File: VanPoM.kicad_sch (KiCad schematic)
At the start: 81 parts, among them IC2 UCC27517DBVR, J1 Socket_ESP32-WROOM-32-NODEMCU, J2 OSTT7020150, J3 OSTT7020150, J4 OSTT7020150, J5 OSTT7020150, Q1 CSD18540Q5B, Q10 CSD18540Q5B, Q2 IPP055N03L G, Q3 IPP120P04P4L03AKSA2, Q4 CSD19531Q5A, Q5 CSD19531Q5A, Q6 CSD19531Q5A, Q7 CSD19531Q5A, Q8 CSD18540Q5B, Q9 CSD18540Q5B, U1 BQ34Z100-R2, U2 LM5109BMA/NOPB, U3 LM5109BMA/NOPB, U4 INA240A2D, U5 INA240A2D, U6 INA240A2D, U7 LM74700, U8 LM74700

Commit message: init
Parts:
- removed J1: Socket_ESP32-WROOM-32-NODEMCU, Connector_PinSocket_2.54mm:PinSocket_1x19_P2.54mm_Vertical, symbol Perso:Socket_ESP32-WROOM-32-NODEMCU
- added C29: 47u, symbol Device:C
- added C30: 10u, symbol Perso:Cv
- added C31: 1u, symbol Perso:Cv
- added C32: 0.022u, symbol Perso:Cv
- added C33: 10n, symbol Device:C
- added C34, C35, C43, C44, C45: 1u, symbol Device:C
- added C36, C37, C38, C39, C40, C41, C42: 0.1u, symbol Device:C
- added D10, D11, D12, D13, D14, D15, D16, D17, D18, D19, D20, D21, D22, D23, D24, D25, D7, D8, D9: PESD2USB3UXT-QR, Package_TO_SOT_SMD:SOT-23, symbol Perso:PESD2USB3UXT-QR
- added D6: B1100B-13-F, symbol Device:D_Schottky
- added IC1: TLV70433DBVT, SOT95P280X145-5N, symbol Perso:TLV70433DBVT
- added IC3: SN74LV4052APWR, Package_SO:TSSOP-16_4.4x5mm_P0.65mm, symbol Perso:SN74LV4052APWR
- added J1: Conn_03x26_Row_Letter_First, Perso:PinHeader_3x25_P2.54mm_Vertical, symbol Perso:Conn_03x26_Row_Letter_First
- added J10: UART3, symbol Connector:Conn_01x04_Pin
- added J11: UART4, symbol Connector:Conn_01x04_Pin
- added J6: OSTT7020150, Perso:CONN2_OSTT7020150_OST, symbol Perso:OSTT7020150
- added J8: UART1, symbol Connector:Conn_01x04_Pin
- added J9: UART2, symbol Connector:Conn_01x04_Pin
- added L3: 220u, symbol Device:L
- added Q11: CSD18540Q5B, Package_TO_SOT_SMD:TDSON-8-1, symbol Transistor_FET:CSD18540Q5B
- added R17: 430k, symbol Device:R
- added R18: 169k, symbol Device:R
- added R19: 3.00k, symbol Device:R
- added R20: 1.00k, symbol Device:R
- added R21: 3.00, symbol Device:R
- added R22, R23, R24, R25: 1.8M, symbol Device:R
- added R26, R27, R28, R29: 200k, symbol Device:R
- added U10: LM5009MM, Package_SO:MSOP-8_3x3mm_P0.65mm, symbol Regulator_Switching:LM5009MM
- added U11: ESP32-S3-DEVKITC-1-N8R2, ESP32-S3-DEVKITC-1-N8R2:XCVR_ESP32-S3-DEVKITC-1-N8R2, symbol Perso:ESP32-S3-DEVKITC-1-N8R2
- added U12: TLA2528IRTER, Perso:WQFN16_RTE_TEX-L, symbol Perso:TLA2528IRTER
- added U13, U14, U15, U16, U17: TVS3300DRV, Package_SON:WSON-6-1EP_2x2mm_P0.65mm_EP1x1.6mm, symbol Perso:TVS3300DRV
- added U9: LM74700, Package_TO_SOT_SMD:SOT-23-6, symbol Power_Management:LM74700
- Q2: value IPP055N03L G -> NX7002AK,215
- Q3: value IPP120P04P4L03AKSA2 -> BSS84W-7-F
- R2: value ~ -> 330k
- R3: value ~ -> 240k
- R4: value ~ -> 390k
- R5: value ~ -> 30k
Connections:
- net +10V: now also C33.1, C34.1, IC1.2 (IN), R21.2
- net +3V3: now also C35.1, D20.1 (K), D20.2 (K), IC1.3 (OUT), IC3.16 (VCC), J1.b1 (Pin_b1), J1.b10 (Pin_b10), J1.b11 (Pin_b11), J1.b12 (Pin_b12), J1.b13 (Pin_b13), J1.b14 (Pin_b14), J1.b15 (Pin_b15), J1.b16 (Pin_b16), J1.b17 (Pin_b17), J1.b18 (Pin_b18), J1.b19 (Pin_b19), J1.b2 (Pin_b2), J1.b20 (Pin_b20), J1.b21 (Pin_b21), J1.b22 (Pin_b22), J1.b23 (Pin_b23), J1.b24 (Pin_b24), J1.b25 (Pin_b25), J1.b26 (Pin_b26), J1.b3 (Pin_b3), J1.b4 (Pin_b4), J1.b5 (Pin_b5), J1.b6 (Pin_b6), J1.b7 (Pin_b7), J1.b8 (Pin_b8), J1.b9 (Pin_b9), J10.1 (Pin_1), J11.1 (Pin_1), J8.1 (Pin_1), J9.1 (Pin_1), U11.J1_1 (3V3), U11.J1_2 (3V3)
- net BAT+: now also R25.1, U16.4 (IN), U16.5 (IN), U16.6 (IN)
- net B_I: now also C40.1, U12.5 (AIN6/GPIO6)
- net Bu_I: now also C41.1, U12.4 (AIN5/GPIO5)
- net GNDREF: now also C30.1, C31.1, C33.2, C34.2, C35.2, C36.2, C37.2, C38.2, C39.2, C40.2, C41.2, C42.2, C43.2, C44.2, C45.2, D21.1 (K), D21.2 (K), D6.2 (A), IC1.1 (GND), IC1.4 (NC_1), IC1.5 (NC_2), IC3.7 (GND_1), IC3.8 (GND_2), J1.a1 (Pin_a1), J1.a10 (Pin_a10), J1.a11 (Pin_a11), J1.a12 (Pin_a12), J1.a13 (Pin_a13), J1.a14 (Pin_a14), J1.a15 (Pin_a15), J1.a16 (Pin_a16), J1.a17 (Pin_a17), J1.a18 (Pin_a18), J1.a19 (Pin_a19), J1.a2 (Pin_a2), J1.a20 (Pin_a20), J1.a21 (Pin_a21), J1.a22 (Pin_a22), J1.a23 (Pin_a23), J1.a24 (Pin_a24), J1.a25 (Pin_a25), J1.a26 (Pin_a26), J1.a3 (Pin_a3), J1.a4 (Pin_a4), J1.a5 (Pin_a5), J1.a6 (Pin_a6), J1.a7 (Pin_a7), J1.a8 (Pin_a8), J1.a9 (Pin_a9), J10.4 (Pin_4), J11.4 (Pin_4), J6.2 (Pin_2), J8.4 (Pin_4), J9.4 (Pin_4), R18.1, R20.2, R26.2, R27.2, R28.2, R29.2, U10.4 (RTN), U11.J1_22 (GND), U11.J3_1 (GND), U11.J3_21 (GND), U11.J3_22 (GND), U12.17 (GND), U12.9 (GND), U17.4 (IN), U17.5 (IN), U17.6 (IN), U9.2 (GND)
- net L_EN: now also U11.J1_15 (GPIO9)
- net P+: now also U13.4 (IN), U13.5 (IN), U13.6 (IN)
- net P_EN: now also U11.J1_18 (GPIO12)
- net P_I: now also C42.1, U12.3 (AIN4/GPIO4)
- net P_S-: now also R24.1
- net SCL: now also U11.J1_17 (GPIO11), U12.14 (SDA)
- net SDA: now also U11.J1_16 (GPIO10), U12.13 (SCL)
- net S_EN: now also U11.J1_19 (GPIO13)
- net V_IN: now also C30.2, Q11.5 (D), R17.1, U10.8 (VIN), U9.4 (CATHODE)
- net V_S: now reaches C20.2, J5.1 (Pin_1), Q8.1 (S), Q8.2 (S), Q8.3 (S), R16.1, U8.6 (ANODE)
- net V_S: now also R22.1, U14.4 (IN), U14.5 (IN), U14.6 (IN)
- new net: L3.2, R19.1, R21.1
- new net: D6.1 (K), R19.2, R20.1, U10.5 (FB)
- new net: C37.1, R24.2, R27.1, U12.1 (AIN2/GPIO2)
- new net: C44.1, U12.10 (DVDD)
- new net: C39.1, R22.2, R29.1, U12.15 (AIN0/GPIO0)
- new net: C38.1, R23.2, R28.1, U12.16 (AIN1/GPIO1)
- new net: C36.1, R25.2, R26.1, U12.2 (AIN3/GPIO3)
- new net: C43.1, U12.7 (AVDD)
- new net: C45.1, U12.8 (DECAP)
- new net: C29.1, U9.1 (VCAP)
- new net: U14.1 (GND), U14.2 (GND), U14.3 (GND), U14.7 (GND)
- new net: C32.1, U10.2 (BST)
- new net: C32.2, L3.1, U10.1 (SW)
- new net: Q11.4 (G), U9.5 (GATE)
- new net: C31.2, U10.7 (VCC)
- new net: R17.2, U10.6 (RON/SD)
- new net: R18.2, U10.3 (RCL)
- new net: U13.1 (GND), U13.2 (GND), U13.3 (GND), U13.7 (GND)
- new net A_EN: U11.J1_20 (GPIO14), U9.3 (EN)
- new net GPIO0: D10.1 (K), J1.c20 (Pin_c20), U11.J3_14 (GPIO0)
- new net GPIO1: D15.1 (K), J1.c10 (Pin_c10), U11.J3_4 (GPIO1)
- new net GPIO15: D18.2 (K), J1.c3 (Pin_c3), U11.J1_8 (GPIO15)
- new net GPIO16: D18.1 (K), J1.c4 (Pin_c4), U11.J1_9 (GPIO16)
- new net GPIO17: D17.2 (K), J1.c5 (Pin_c5), U11.J1_10 (GPIO17)
- new net GPIO18: D17.1 (K), J1.c6 (Pin_c6), U11.J1_11 (GPIO18)
- new net GPIO19: D7.1 (K), J1.c26 (Pin_c26), U11.J3_20 (USB_D-/GPIO19)
- new net GPIO2: D14.2 (K), J1.c11 (Pin_c11), U11.J3_5 (GPIO2)
- new net GPIO20: D7.2 (K), J1.c25 (Pin_c25), U11.J3_19 (USB_D+/GPIO20)
- new net GPIO21: D8.1 (K), J1.c24 (Pin_c24), U11.J3_18 (GPIO21)
- new net GPIO3: D16.1 (K), J1.c8 (Pin_b8), U11.J1_13 (GPIO3)
- new net GPIO35: D10.2 (K), J1.c19 (Pin_c19), U11.J3_13 (GPIO35)
- new net GPIO36: D11.1 (K), J1.c18 (Pin_c18), U11.J3_12 (GPIO36)
- new net GPIO37: D11.2 (K), J1.c17 (Pin_c17), U11.J3_11 (GPIO37)
- new net GPIO38: D12.1 (K), J1.c16 (Pin_c16), U11.J3_10 (GPIO38)
- new net GPIO39: D12.2 (K), J1.c15 (Pin_c15), U11.J3_9 (MTCK/GPIO39)
- new net GPIO40: D13.1 (K), J1.c14 (Pin_c14), U11.J3_8 (MTDO/GPIO40)
- new net GPIO41: D13.2 (K), J1.c13 (Pin_c13), U11.J3_7 (MTDI/GPIO41)
- new net GPIO42: D14.1 (K), J1.c12 (Pin_c12), U11.J3_6 (MTMS/GPIO42)
- new net GPIO45: D9.2 (K), J1.c21 (Pin_c21), U11.J3_15 (GPIO45)
- new net GPIO46: D15.2 (K), J1.c9 (Pin_c9), U11.J1_14 (GPIO46)
- new net GPIO47: D8.2 (K), J1.c23 (Pin_c23), U11.J3_17 (GPIO47)
- new net GPIO48: D9.1 (K), J1.c22 (Pin_c22), U11.J3_16 (GPIO48)
- new net GPIO6: D19.2 (K), J1.c1 (Pin_c1), U11.J1_6 (GPIO6)
- new net GPIO7: D19.1 (K), J1.c2 (Pin_c2), U11.J1_7 (GPIO7)
- new net GPIO8: D16.2 (K), J1.c7 (Pin_b7), U11.J1_12 (GPIO8)
- new net RX0: IC3.12 (1Y0)
- new net RX1: D22.2 (K), IC3.14 (1Y1), J8.2 (Pin_2)
- new net RX2: D23.2 (K), IC3.15 (1Y2), J9.2 (Pin_2)
- new net RX3: D24.2 (K), IC3.11 (1Y3), J10.2 (Pin_2)
- new net RX4: D25.2 (K), J11.2 (Pin_2)
- new net RX_COM: IC3.13 (1-COM), U11.J3_3 (U0RXD/GPIO44)
- new net TVS: U15.1 (GND), U15.2 (GND), U15.3 (GND), U15.7 (GND), U16.1 (GND), U16.2 (GND), U16.3 (GND), U16.7 (GND), U17.1 (GND), U17.2 (GND), U17.3 (GND), U17.7 (GND)
- new net TVS_3v3: D10.3 (A), D11.3 (A), D12.3 (A), D13.3 (A), D14.3 (A), D15.3 (A), D16.3 (A), D17.3 (A), D18.3 (A), D19.3 (A), D20.3 (A), D21.3 (A), D22.3 (A), D23.3 (A), D24.3 (A), D25.3 (A), D7.3 (A), D8.3 (A), D9.3 (A)
- new net TX0: IC3.1 (2Y0)
- new net TX1: D22.1 (K), IC3.5 (2Y1), J8.3 (Pin_3)
- new net TX2: D23.1 (K), IC3.2 (2Y2), J9.3 (Pin_3)
- new net TX3: D24.1 (K), IC3.4 (2Y3), J10.3 (Pin_3)
- new net TX4: D25.1 (K), J11.3 (Pin_3)
- new net TX_COM: IC3.3 (2-COM), U11.J3_2 (U0TXD/GPIO43)
- new net UART_A0: IC3.10 (A), U11.J1_4 (GPIO4)
- new net UART_A1: IC3.9 (B), U11.J1_5 (GPIO5)
- new net V_A: C29.2, J6.1 (Pin_1), Q11.1 (S), Q11.2 (S), Q11.3 (S), R23.1, U15.4 (IN), U15.5 (IN), U15.6 (IN), U9.6 (ANODE)
- no-connect marks 0 -> 2
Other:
- note added: "Car generator"
- moved on the sheet: C1, C10, C11, C12, C13, C14, C15, C16, C17, C18, C19, C2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

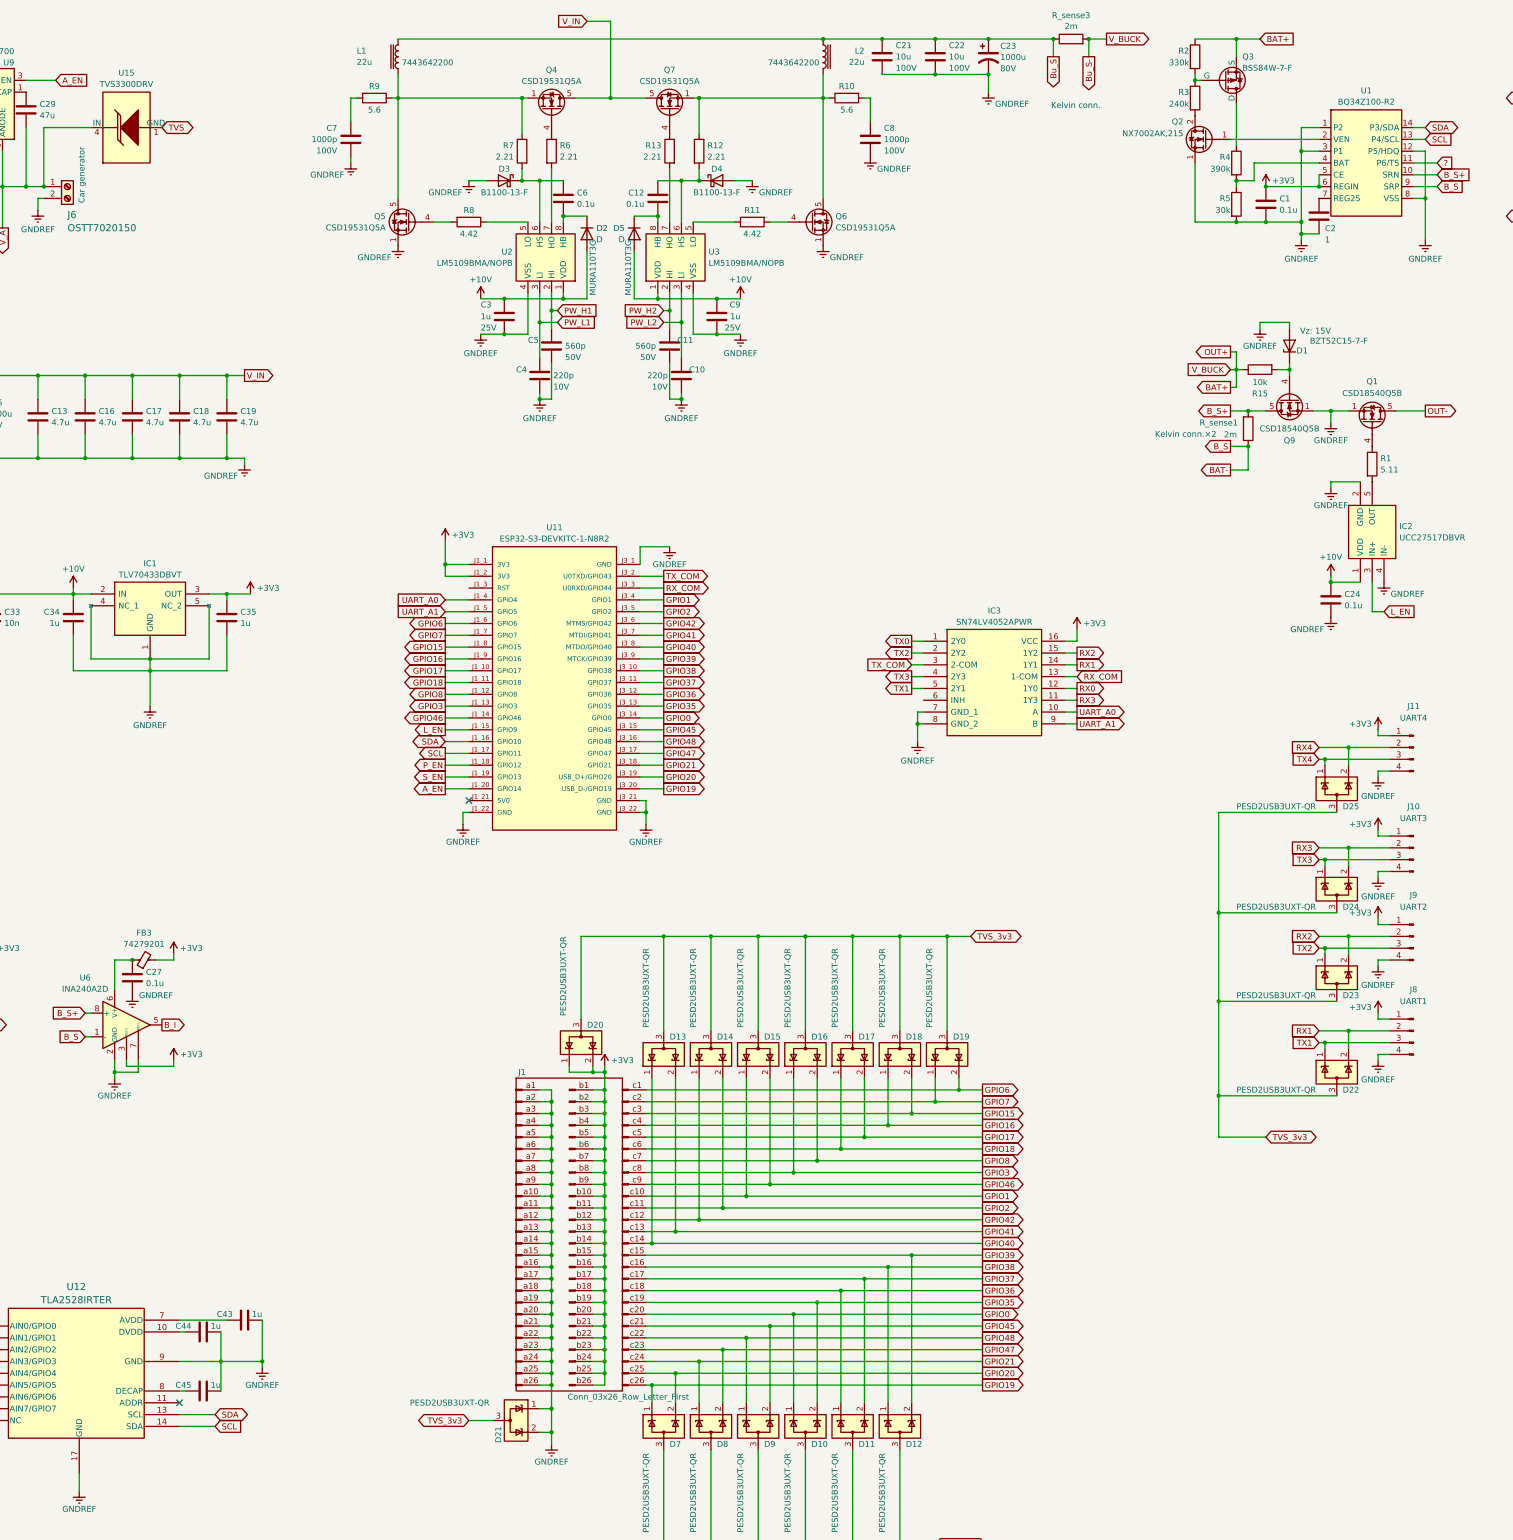
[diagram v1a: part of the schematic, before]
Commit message: + pull ups I²C; f sda scl swaped on U12; + I²C addrs; + I²C connector
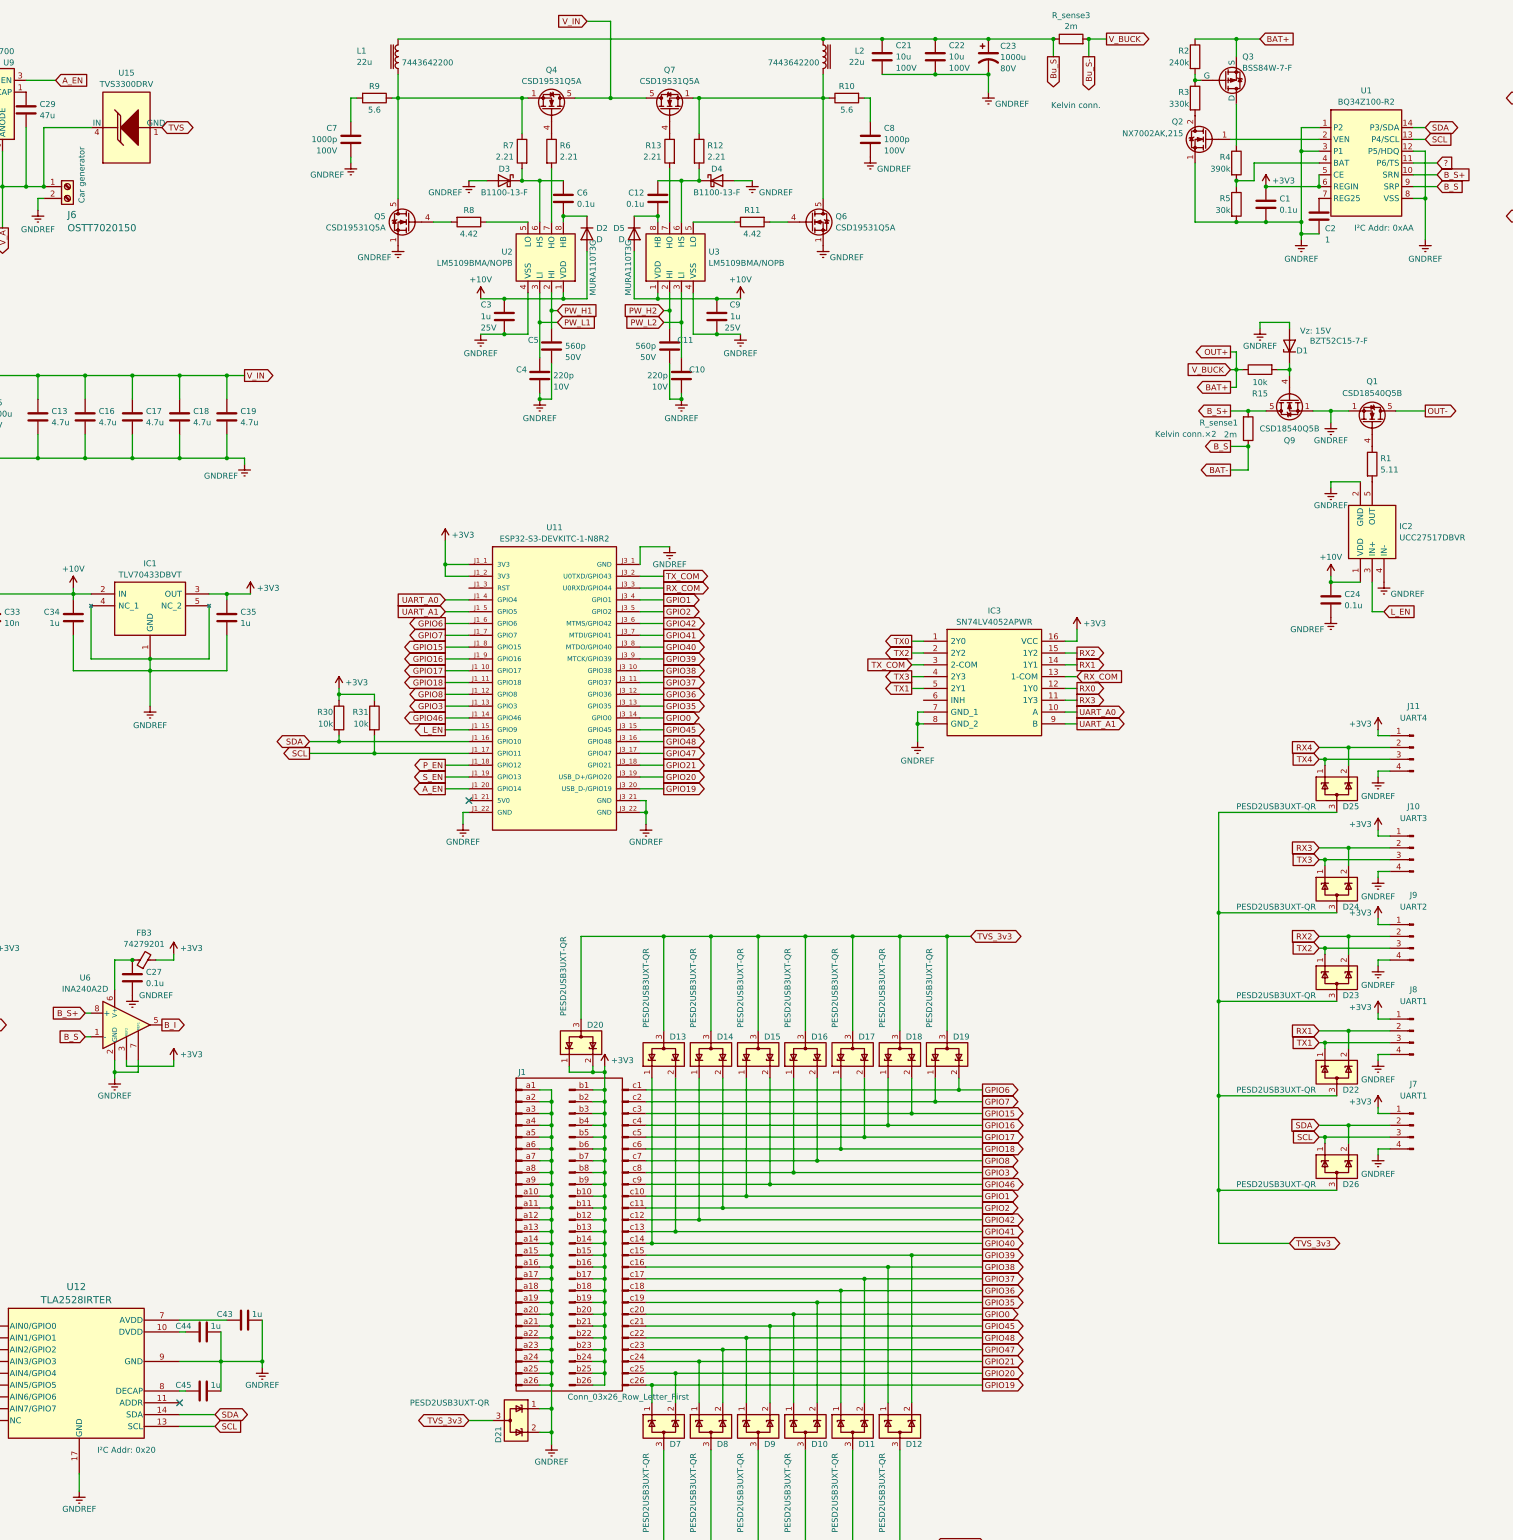
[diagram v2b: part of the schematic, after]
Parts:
- added D26: PESD2USB3UXT-QR, Package_TO_SOT_SMD:SOT-23, symbol Perso:PESD2USB3UXT-QR
- added J7: UART1, symbol Connector:Conn_01x04_Pin
- added R30, R31: 10k, symbol Device:R
- R2: value 330k -> 240k
- R3: value 240k -> 330k
- U1: I²C Addr (none) -> 0xAA
- U12: I²C Addr (none) -> 0x20
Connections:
- net +3V3: now also J7.1 (Pin_1), R30.1, R31.1
- net GNDREF: now also J7.4 (Pin_4)
- net SCL: now also U12.13 (SCL), D26.1 (K), J7.3 (Pin_3), R31.2; no longer U12.14 (SDA)
- net SDA: now also U12.14 (SDA), D26.2 (K), J7.2 (Pin_2), R30.2; no longer U12.13 (SCL)
- net TVS_3v3: now also D26.3 (A)
